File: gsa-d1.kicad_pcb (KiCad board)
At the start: 2 copper layers, 100 x 100 mm, 94 parts, among them J201 CONN-2, J202 CONN-4, J203 CONN-2, J301 CONN-4, J302 CONN-3, J303 CONN-3, J304 CONN-3, J305 CONN-3, J306 CONN-3, J307 CONN-2, J308 CONN-3, J401 CONN-3, J402 CONN-2, J403 CONN-3, J404 CONN-2, Q201 2N7000, Q202 2N7000, Q203 2N7000, Q204 2N7000, Q205 2N7000, SW201 SP-PUSH, SW202 SP-PUSH, SW203 SP-PUSH, SW204 SP-PUSH, SW205 SP-PUSH, U201 4093, U202 4017, U301 4066, U302 4066, U303 7905, U304 7805, U401 LM1876, X301 LINK, X302 LINK

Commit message: Minor layout improvements to pre-amp controls
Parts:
- moved R301 15.9 mm to (126.4, 55.9)
- moved R302 15.9 mm to (142.2, 55.9)
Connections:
- net /Inputs and Pre-Amp/A renamed /A
- net /Inputs and Pre-Amp/A-L renamed /A-L
- net /Inputs and Pre-Amp/A-R renamed /A-R
- net /Inputs and Pre-Amp/B renamed /B
- net /Inputs and Pre-Amp/B-L renamed /B-L
- net /Inputs and Pre-Amp/B-R renamed /B-R
- net /Inputs and Pre-Amp/C renamed /C
- net /Inputs and Pre-Amp/C-L renamed /C-L
- net /Inputs and Pre-Amp/C-R renamed /C-R
- net /Inputs and Pre-Amp/D renamed /D
- net /Inputs and Pre-Amp/D-L renamed /D-L
- net /Inputs and Pre-Amp/D-R renamed /D-R
- net /Inputs and Pre-Amp/GND-P renamed /GND-P
- net /Inputs and Pre-Amp/GND-S renamed /GND-S
- net /Inputs and Pre-Amp/V+ renamed /V+
- net /Inputs and Pre-Amp/V- renamed /V-
- net /Inputs and Pre-Amp/Vin+ renamed /Vin+
- net /Inputs and Pre-Amp/Vin- renamed /Vin-
- J308 pad 1: /Inputs and Pre-Amp/L-Out -> /L-Out
- J308 pad 3: /Inputs and Pre-Amp/R-Out -> /R-Out
- R301 pad 1: /Inputs and Pre-Amp/L-Out -> /L-Out
- R302 pad 2: /Inputs and Pre-Amp/R-Out -> /R-Out
- U301 pad 10: /Inputs and Pre-Amp/R -> /R
- U301 pad 2: /Inputs and Pre-Amp/L -> /L
- U301 pad 3: /Inputs and Pre-Amp/L -> /L
- U301 pad 9: /Inputs and Pre-Amp/R -> /R
- U302 pad 10: /Inputs and Pre-Amp/R -> /R
- U302 pad 2: /Inputs and Pre-Amp/L -> /L
- U302 pad 3: /Inputs and Pre-Amp/L -> /L
- U302 pad 9: /Inputs and Pre-Amp/R -> /R
- VR302 pad 2: /Inputs and Pre-Amp/L-Out -> /R-Out
- VR302 pad 3: /Inputs and Pre-Amp/L -> /R
- VR302 pad 5: /Inputs and Pre-Amp/R-Out -> /L-Out
- VR302 pad 6: /Inputs and Pre-Amp/R -> /L
- X301 pad 2: /Inputs and Pre-Amp/L -> /L
- X302 pad 2: /Inputs and Pre-Amp/R -> /R
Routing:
- net /Inputs and Pre-Amp/L: track 74.0 -> 0.00 mm
- net /R: track 0.00 -> 73.9 mm
- net /L: track 0.00 -> 69.4 mm
- net /Inputs and Pre-Amp/R: track 67.4 -> 0.00 mm
- net /Inputs and Pre-Amp/L-Out: track 56.9 -> 0.00 mm, vias 1 -> 0
- net /R-Out: track 0.00 -> 56.8 mm, vias 0 -> 1
- net /Inputs and Pre-Amp/R-Out: track 34.3 -> 0.00 mm, vias 1 -> 0
- net /L-Out: track 0.00 -> 33.3 mm, vias 0 -> 1
- net Net-(R301-Pad2): track 9.51 -> 27.8 mm
- net Net-(R302-Pad1): track 40.1 -> 23.1 mm
- net /Vin+: track 14.0 -> 12.7 mm
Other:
- board text added: "GSA-D1-S201 © T J Baldwin 2016,2018"

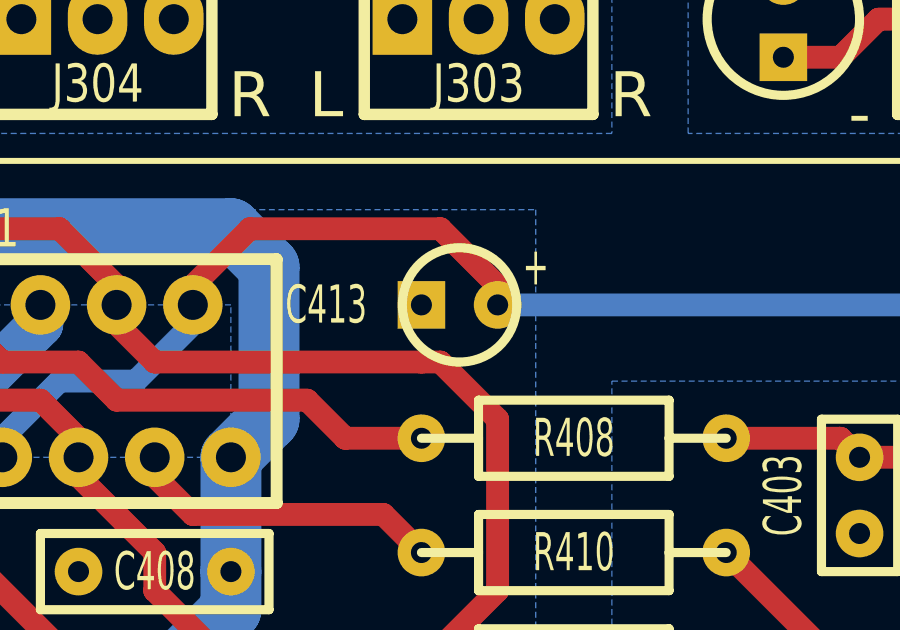
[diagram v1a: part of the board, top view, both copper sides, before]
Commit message: Reduce size of power supply PCB
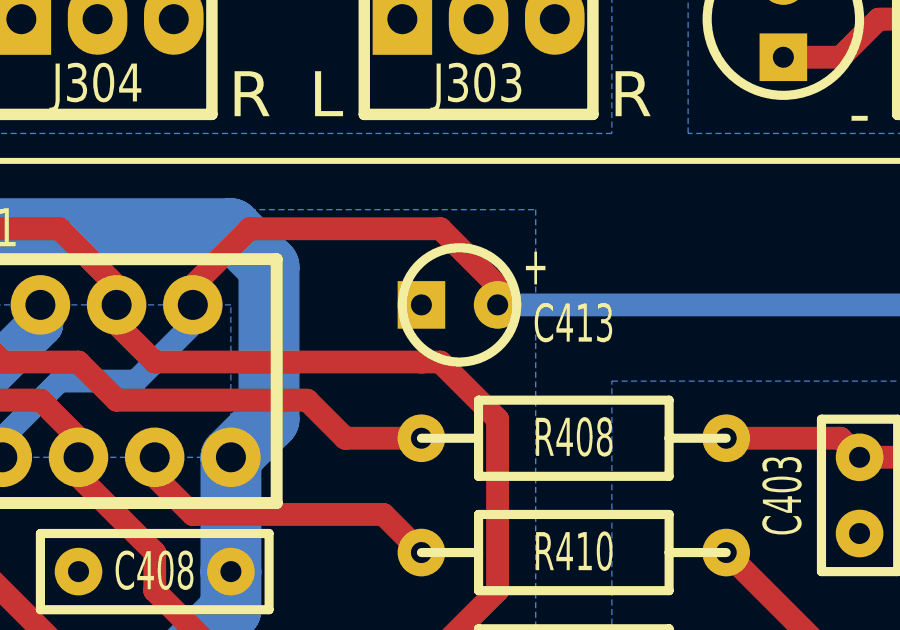
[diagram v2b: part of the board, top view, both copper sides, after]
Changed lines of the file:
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@@
     (links 227)
     (no_connects 0)
-    (area 99.619999 50.724999 199.770001 150.875001)
+    (area 98.32975 38.915999 199.770001 151.86025)
     (thickness 1.6)
     (drawings 64)
@@
   (module gsa:ELEC4R (layer F.Cu)
     (at 162.56 88.9 180)
-    (fp_text reference C413 (at 4.445 0 360) (layer F.SilkS)
-      (effects (font (size 1.27 0.762) (thickness 0.1905)))
-    )
+    (fp_text reference C413 (at -3.81 -0.635 360) (layer F.SilkS)
+      (effects (font (size 1.27 0.762) (thickness 0.1905)))
+    )

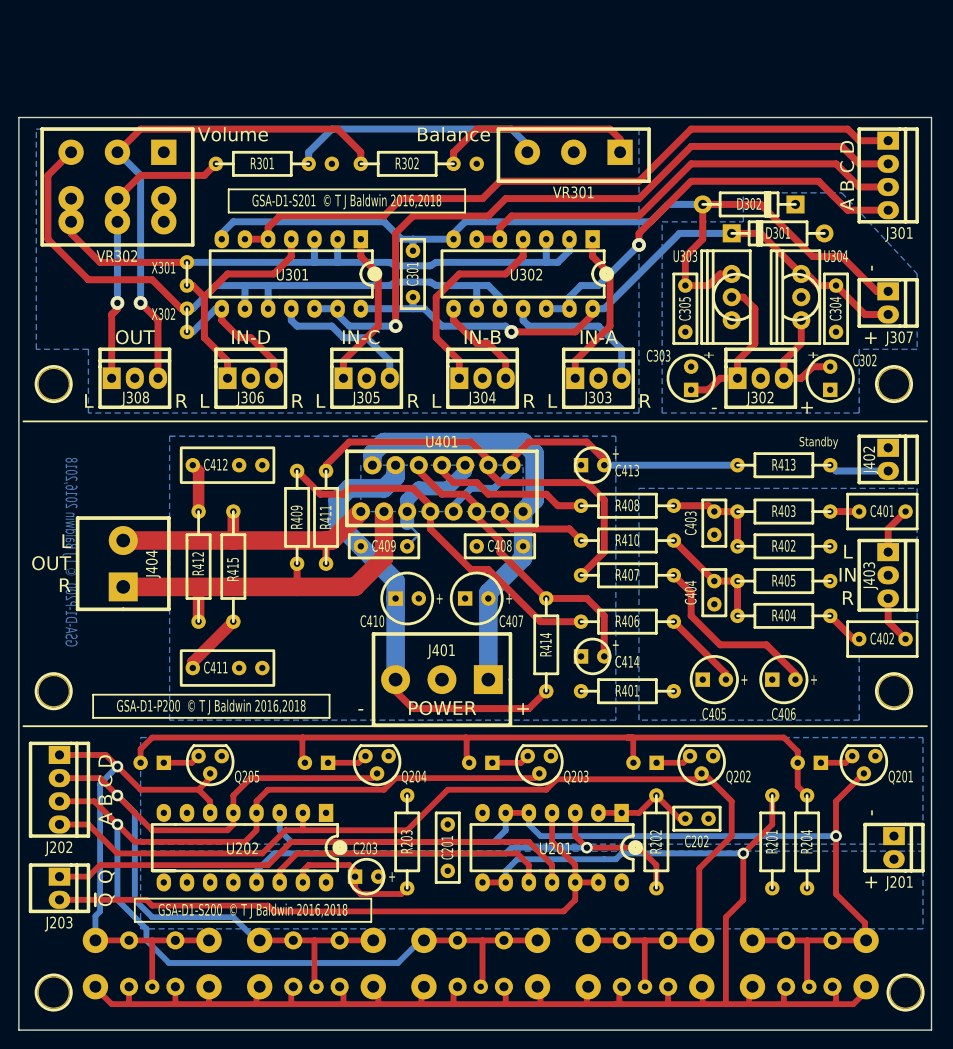
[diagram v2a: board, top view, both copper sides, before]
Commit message: Updated to use KiCad v5
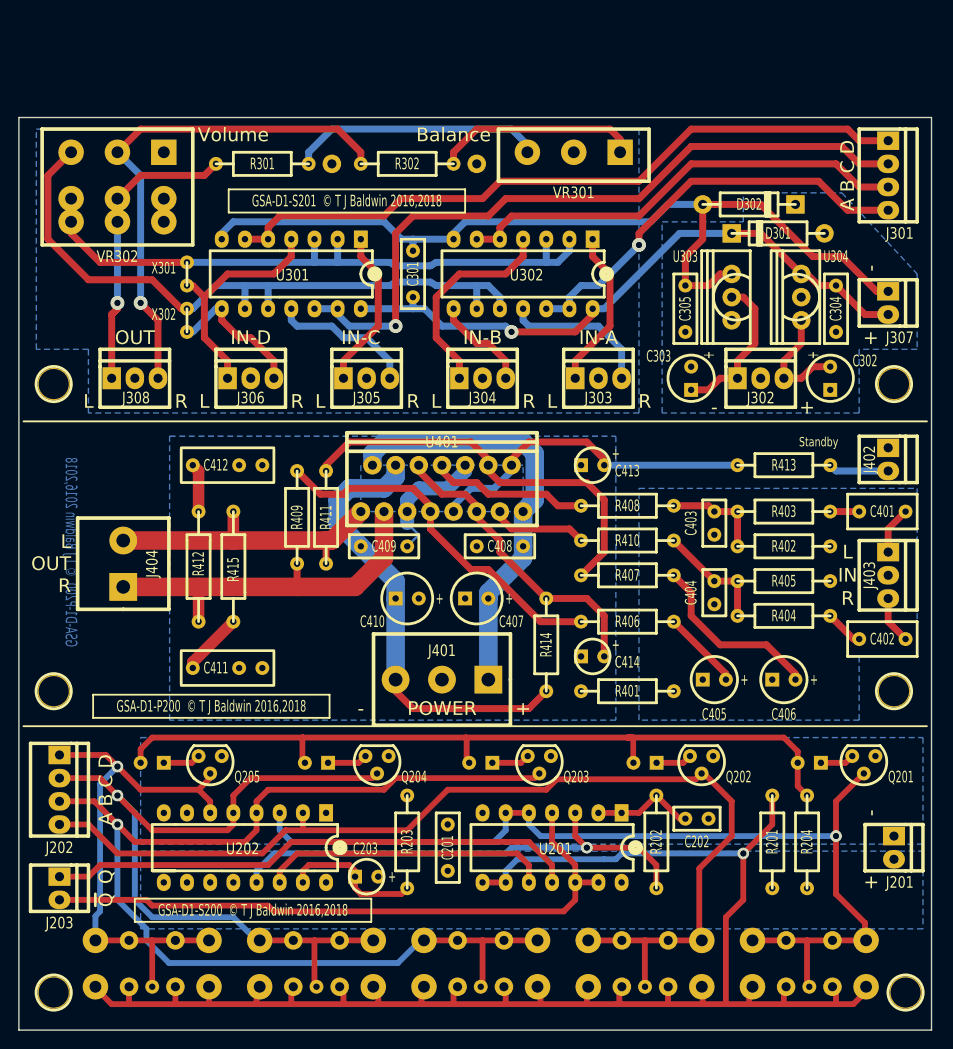
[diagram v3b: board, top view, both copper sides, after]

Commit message: Updated to use gsa-lib v1.1
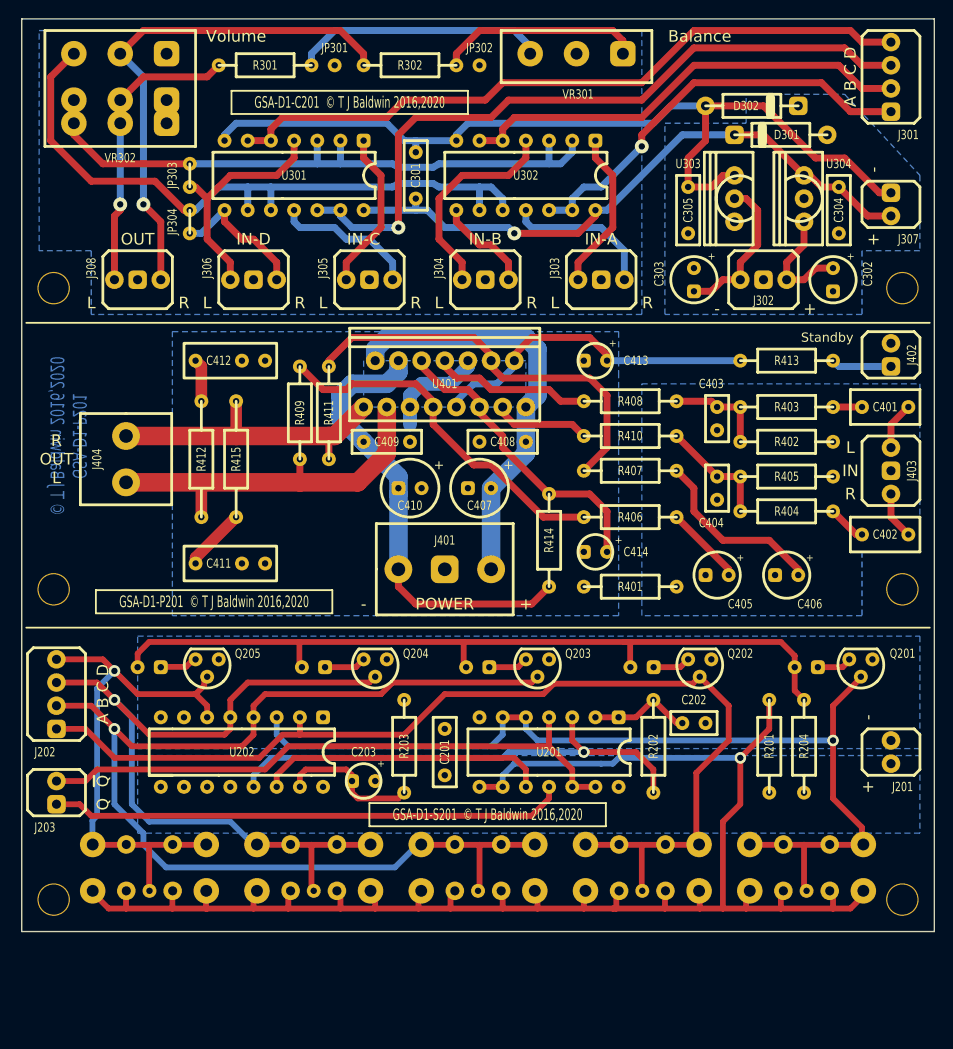
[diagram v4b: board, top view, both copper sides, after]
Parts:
- removed PAD-S (x2): VAL**, gsa:PAD-S
- removed X301, X302: LINK, gsa:LINK2
- added JP301: PAD, gsa:PAD07, F.Cu at (134.3, 45.1)
- added JP302: PAD, gsa:PAD07, F.Cu at (150.2, 45.1)
- added JP303: LINK, gsa:LINK2, F.Cu at (118.4, 57.1)
- added JP304: LINK, gsa:LINK2, F.Cu at (118.4, 62.2)
- C411, C412: footprint gsa:CAP-5-7 -> gsa:CAP-7-10
- SW201, SW202, SW203, SW204, SW205: value SP-PUSH -> SW-PUSH; footprint gsa:SW-TACT2 -> gsa:SW-TACT-ALL
- moved R412 12.1 mm to (119.7, 88.2)
- moved C407 12.1 mm to (150.2, 91.4), turned to 0 degrees
- moved C410 12.1 mm to (142.5, 91.4), turned to 0 degrees
- moved J401 12.1 mm to (146.4, 100.3), turned to 0 degrees
- moved Q201 11.9 mm to (191.9, 110.2), turned to 180 degrees
- moved Q205 11.9 mm to (120.3, 110.2), turned to 180 degrees
- moved Q202 11.9 mm to (174.3, 110.2), turned to 180 degrees
- moved Q203 11.9 mm to (156.5, 110.2), turned to 180 degrees
- moved Q204 11.9 mm to (138.7, 110.2), turned to 180 degrees
- moved C408 11.5 mm to (152.7, 86.3), turned to 180 degrees
- moved C409 11.5 mm to (140.0, 86.3), turned to 0 degrees
- moved C412 11.5 mm to (122.9, 77.4)
- moved C413 11.5 mm to (162.9, 77.4), turned to 0 degrees
- moved R401 11.5 mm to (166.7, 102.2)
- moved R402 11.5 mm to (183.8, 86.3)
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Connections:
- net /GND-S renamed /Inputs and Pre-Amp/GND-S
- net /Input Selector/Clock renamed /Clock
- net /Input Selector/Enable renamed /Enable
- net /Input Selector/Q renamed /Q
- net /Input Selector/~Q renamed /~Q
- net /L renamed /Inputs and Pre-Amp/L
- net /R renamed /Inputs and Pre-Amp/R
- C201 pad 1: /Input Selector/V+ -> /V-
- C201 pad 2: /Input Selector/V- -> /V+
- C202 pad 1: Net-(C202-Pad1) -> /V-
- C202 pad 2: /Input Selector/V- -> Net-(C202-Pad2)
- C203 pad 1: /Input Selector/V+ -> /Reset
- C203 pad 2: /Input Selector/Reset -> /V+
- C301 pad 1: /V+ -> /Inputs and Pre-Amp/V-
- C301 pad 2: /V- -> /Inputs and Pre-Amp/V+
- C302 pad 1: /Vin+ -> /Inputs and Pre-Amp/GND-P
- C302 pad 2: /GND-P -> /Inputs and Pre-Amp/Vin+
- C303 pad 1: /GND-P -> /Inputs and Pre-Amp/Vin-
- C303 pad 2: /Vin- -> /Inputs and Pre-Amp/GND-P
- C304 pad 1: /V+ -> /Inputs and Pre-Amp/GND-P
- C304 pad 2: /GND-P -> /Inputs and Pre-Amp/V+
- C305 pad 1: /GND-P -> /Inputs and Pre-Amp/V-
- C305 pad 2: /V- -> /Inputs and Pre-Amp/GND-P
- C401 pad 1: Net-(C401-Pad1) -> /Power Amp/L-In
- C401 pad 2: /Power Amp/L-In -> Net-(C401-Pad2)
- C402 pad 1: Net-(C402-Pad1) -> /Power Amp/R-In
- C402 pad 2: /Power Amp/R-In -> Net-(C402-Pad2)
- C403 pad 1: /Power Amp/GND-S -> Net-(C403-Pad1)
- C403 pad 2: Net-(C403-Pad2) -> /Power Amp/GND-S
- C404 pad 1: /Power Amp/GND-S -> Net-(C404-Pad1)
- C404 pad 2: Net-(C404-Pad2) -> /Power Amp/GND-S
- C405 pad 1: Net-(C405-Pad1) -> /Power Amp/GND-S
- C405 pad 2: /Power Amp/GND-S -> Net-(C405-Pad2)
- C406 pad 1: Net-(C406-Pad1) -> /Power Amp/GND-S
- C406 pad 2: /Power Amp/GND-S -> Net-(C406-Pad2)
- C407 pad 1: /Power Amp/V+ -> GND
- C407 pad 2: GND -> /Power Amp/V+
- C408 pad 1: GND -> /Power Amp/V+
- C408 pad 2: /Power Amp/V+ -> GND
- C409 pad 1: GND -> /Power Amp/V-
- C409 pad 2: /Power Amp/V- -> GND
- C410 pad 1: GND -> /Power Amp/V-
- C410 pad 2: /Power Amp/V- -> GND
- C413 pad 1: /Power Amp/SB -> GND
- C413 pad 2: GND -> /Power Amp/SB
- C414 pad 1: /Power Amp/MT -> GND
- C414 pad 2: GND -> /Power Amp/MT
- J201 pad 1: /Input Selector/V- -> /V-
- J201 pad 2: /Input Selector/V+ -> /V+
- J202 pad 1: /Input Selector/D -> /A
- J202 pad 2: /Input Selector/C -> /B
- J202 pad 3: /Input Selector/B -> /C
- J202 pad 4: /Input Selector/A -> /D
- J301 pad 1: /D -> /Inputs and Pre-Amp/A
- J301 pad 2: /C -> /Inputs and Pre-Amp/B
- J301 pad 3: /B -> /Inputs and Pre-Amp/C
- J301 pad 4: /A -> /Inputs and Pre-Amp/D
- J302 pad 1: /Vin- -> /Inputs and Pre-Amp/Vin-
- J302 pad 2: /GND-P -> /Inputs and Pre-Amp/GND-P
- J302 pad 3: /Vin+ -> /Inputs and Pre-Amp/Vin+
- J303 pad 1: /A-L -> /Inputs and Pre-Amp/A-R
- J303 pad 3: /A-R -> /Inputs and Pre-Amp/A-L
- J304 pad 1: /B-L -> /Inputs and Pre-Amp/B-R
- J304 pad 3: /B-R -> /Inputs and Pre-Amp/B-L
- J305 pad 1: /C-L -> /Inputs and Pre-Amp/C-R
- J305 pad 3: /C-R -> /Inputs and Pre-Amp/C-L
- J306 pad 1: /D-L -> /Inputs and Pre-Amp/D-R
- J306 pad 3: /D-R -> /Inputs and Pre-Amp/D-L
- J307 pad 1: /V- -> /Inputs and Pre-Amp/V-
- J307 pad 2: /V+ -> /Inputs and Pre-Amp/V+
- J308 pad 1: /L-Out -> /Inputs and Pre-Amp/R-Out
- J308 pad 3: /R-Out -> /Inputs and Pre-Amp/L-Out
- J401 pad 1: /Power Amp/V+ -> /Power Amp/V-
- J401 pad 3: /Power Amp/V- -> /Power Amp/V+
- J402 pad 1: (no net) -> /Power Amp/Standby
- J402 pad 2: /Power Amp/Standby -> Net-(J402-Pad2)
- J403 pad 1: /Power Amp/L-In -> /Power Amp/R-In
- J403 pad 3: /Power Amp/R-In -> /Power Amp/L-In
- J404 pad 1: /Power Amp/L-Out -> /Power Amp/R-Out
- J404 pad 2: /Power Amp/R-Out -> /Power Amp/L-Out
- R201 pad 2: /Input Selector/V+ -> /V+
- R202 pad 2: Net-(C202-Pad1) -> Net-(C202-Pad2)
- R203 pad 1: /Input Selector/V- -> /V-
- R203 pad 2: /Input Selector/Reset -> /Reset
- R204 pad 1: /Input Selector/V+ -> /V+
- R204 pad 2: Net-(D201-PadA) -> Net-(D201-Pada)
- R301 pad 1: /L-Out -> /Inputs and Pre-Amp/L-Out
- R302 pad 2: /R-Out -> /Inputs and Pre-Amp/R-Out
- R402 pad 1: Net-(C403-Pad2) -> Net-(C403-Pad1)
- R403 pad 1: Net-(C401-Pad1) -> Net-(C401-Pad2)
- R403 pad 2: Net-(C403-Pad2) -> Net-(C403-Pad1)
- R404 pad 1: Net-(C402-Pad1) -> Net-(C402-Pad2)
- R404 pad 2: Net-(C404-Pad2) -> Net-(C404-Pad1)
- R405 pad 1: Net-(C404-Pad2) -> Net-(C404-Pad1)
- R406 pad 2: Net-(C405-Pad1) -> Net-(C405-Pad2)
- R407 pad 2: Net-(C406-Pad1) -> Net-(C406-Pad2)
- R408 pad 1: Net-(C403-Pad2) -> Net-(C403-Pad1)
- R410 pad 1: Net-(C404-Pad2) -> Net-(C404-Pad1)
- SW201 pad 1: /Input Selector/Q0 -> /Q0
- SW202 pad 1: /Input Selector/A -> /A
- SW203 pad 1: /Input Selector/B -> /B
- SW204 pad 1: /Input Selector/C -> /C
- SW205 pad 1: /Input Selector/D -> /D
- U201 pad 1: Net-(C202-Pad1) -> Net-(C202-Pad2)
- U201 pad 14: /Input Selector/V+ -> /V+
- U201 pad 2: Net-(C202-Pad1) -> Net-(C202-Pad2)
- U201 pad 5: /Input Selector/Q0 -> /Q0
- U201 pad 6: /Input Selector/Q0 -> /Q0
- U201 pad 7: /Input Selector/V- -> /V-
- U202 pad 1: (no net) -> Net-(U202-Pad1)
- U202 pad 10: (no net) -> Net-(U202-Pad10)
- U202 pad 11: (no net) -> Net-(U202-Pad11)
- U202 pad 12: (no net) -> Net-(U202-Pad12)
- U202 pad 15: /Input Selector/Reset -> /Reset
- U202 pad 16: /Input Selector/V+ -> /V+
- U202 pad 2: /Input Selector/A -> /A
- U202 pad 3: /Input Selector/Q0 -> /Q0
- U202 pad 4: /Input Selector/B -> /B
- U202 pad 5: /Input Selector/C -> /C
- U202 pad 6: /Input Selector/D -> /D
- U202 pad 7: (no net) -> Net-(U202-Pad7)
- U202 pad 8: /Input Selector/V- -> /V-
- U202 pad 9: (no net) -> Net-(U202-Pad9)
- U301 pad 1: /C-L -> /Inputs and Pre-Amp/C-L
- U301 pad 11: /C-R -> /Inputs and Pre-Amp/C-R
- U301 pad 12: /C -> /Inputs and Pre-Amp/C
- U301 pad 13: /C -> /Inputs and Pre-Amp/C
- U301 pad 14: /V+ -> /Inputs and Pre-Amp/V+
- U301 pad 4: /D-L -> /Inputs and Pre-Amp/D-L
- U301 pad 5: /D -> /Inputs and Pre-Amp/D
- U301 pad 6: /D -> /Inputs and Pre-Amp/D
- U301 pad 7: /V- -> /Inputs and Pre-Amp/V-
- U301 pad 8: /D-R -> /Inputs and Pre-Amp/D-R
- U302 pad 1: /A-L -> /Inputs and Pre-Amp/A-L
- U302 pad 11: /A-R -> /Inputs and Pre-Amp/A-R
- U302 pad 12: /A -> /Inputs and Pre-Amp/A
- U302 pad 13: /A -> /Inputs and Pre-Amp/A
- U302 pad 14: /V+ -> /Inputs and Pre-Amp/V+
- U302 pad 4: /B-L -> /Inputs and Pre-Amp/B-L
- U302 pad 5: /B -> /Inputs and Pre-Amp/B
- U302 pad 6: /B -> /Inputs and Pre-Amp/B
- U302 pad 7: /V- -> /Inputs and Pre-Amp/V-
- U302 pad 8: /B-R -> /Inputs and Pre-Amp/B-R
- U303 pad 1: /GND-P -> /Inputs and Pre-Amp/GND-P
- U303 pad 2: /Vin- -> /Inputs and Pre-Amp/Vin-
- U303 pad 3: /V- -> /Inputs and Pre-Amp/V-
- U304 pad 1: /Vin+ -> /Inputs and Pre-Amp/Vin+
- U304 pad 2: /GND-P -> /Inputs and Pre-Amp/GND-P
- U304 pad 3: /V+ -> /Inputs and Pre-Amp/V+
- VR302 pad 2: /R-Out -> /Inputs and Pre-Amp/R-Out
- VR302 pad 5: /L-Out -> /Inputs and Pre-Amp/L-Out
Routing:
- net /Input Selector/B: track 123.7 -> 0.00 mm, vias 1 -> 0
- net /Input Selector/A: track 116.0 -> 0.00 mm
- net /Input Selector/Q0: track 106.3 -> 0.00 mm, vias 1 -> 0
- net /Q0: track 0.00 -> 106.3 mm, vias 0 -> 1
- net /V-: track 98.1 -> 0.00 mm
- net /Inputs and Pre-Amp/V-: track 0.00 -> 97.4 mm
- net Net-(D201-PadA): track 89.7 -> 0.00 mm
- net Net-(D201-Pada): track 0.00 -> 89.7 mm
- net /Input Selector/C: track 86.8 -> 0.00 mm, vias 1 -> 0
- net /Inputs and Pre-Amp/C: track 0.00 -> 78.9 mm, vias 0 -> 1
- net /Inputs and Pre-Amp/D: track 0.00 -> 76.8 mm
- net /B: track 50.3 -> 123.7 mm, vias 0 -> 1
- net /A: track 46.1 -> 116.0 mm, vias 1 -> 0
- net /Inputs and Pre-Amp/V+: track 0.00 -> 68.6 mm, vias 0 -> 1
- net /V+: track 68.0 -> 0.00 mm, vias 1 -> 0
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- added copper zone on B.Cu, net /Inputs and Pre-Amp/GND-P
- added copper zone on B.Cu, net /V+
- added copper zone on B.Cu, net /V-
- removed copper zone on B.Cu, net /GND-P
- removed copper zone on B.Cu, net /Input Selector/V+
- removed copper zone on B.Cu, net /Input Selector/V-
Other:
- net class Default: clearance 0.254 -> 0.2; trace_width 0.762 -> 0.25; via_dia 1.524 -> 0.8; via_drill 0.7 -> 0.4
- rule pad_to_mask_clearance: 0.2 -> 0.05
- rule trace_clearance: 0.254 -> 0.2
- board text added: "GSA-D1-C201 © T J Baldwin 2016,2020"
- board text added: "GSA-D1-P201 © T J Baldwin 2016,2020"
- board text added: "GSA-D1-S201 © T J Baldwin 2016,2020"
- board text added: "R OUT L"
- board text removed: "GSA-D1-P200 © T J Baldwin 2016,2018"
- board text removed: "GSA-D1-S200 © T J Baldwin 2016,2018"
- board text removed: "GSA-D1-S201 © T J Baldwin 2016,2018"
- board text removed: "L OUT R"
